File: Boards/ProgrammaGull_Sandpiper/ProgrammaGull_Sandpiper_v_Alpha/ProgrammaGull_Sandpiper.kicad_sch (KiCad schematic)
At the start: 190 parts, among them J4 Conn_01x22_Socket, P1 USB_C_Plug_USB2.0, Q1 MMBT2907, Q2 MMBT2907, Q3 MMBT2907, Q4 MMBT2907, Q5 MMBT2907, Q6 MMBT2907, Q7 MMBT2907, Q8 MMBT2907, SW10 SW_Push, SW11 SW_Push, SW12 SW_Push, SW14 SW_Push, SW9 SW_Push, U1 ICE40UP5K-SG48ITR, U11 ADC084S051CIMM/NOPB, U12 74HC596, U13 74AHC595, U14 W25Q32JVSS, U15 AMS1117-3.3, U2 SN74LVC1G126DCKR, U3 74HC596, U4 MIC5504-1.2YM5, U5 MIC5504-2.5YM5, U6 93LCxxAxxOT, U7 FT2232HQ, X1 SG-210STF

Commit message: Final Alpha Version
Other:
- note added: "Digikey/Mouser: CLMVC-FKA-CLBDGL7LBB79353 JLC/LCSC Option: NH-Z1921RGBA-SF"
- note added: "JLC/LCSC Alternate: YM4012M00033T8188099"
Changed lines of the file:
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@@
+    (effects (font (size 1.27 1.27)) (justify left bottom))
+  )
+  (text "Digikey/Mouser: CLMVC-FKA-CLBDGL7LBB79353\nJLC/LCSC Option: NH-Z1921RGBA-SF"
+    (at 17.78 332.74 0)
     (effects (font (size 1.27 1.27)) (justify left bottom))
   )
@@
     (effects (font (size 3 3)) (justify left bottom))
   )
+  (text "JLC/LCSC Alternate: YM4012M00033T8188099" (at 575.31 99.06 0)
+    (effects (font (size 1.27 1.27)) (justify left bottom))
+  )
   (text "D Pad" (at 405.13 266.065 0)

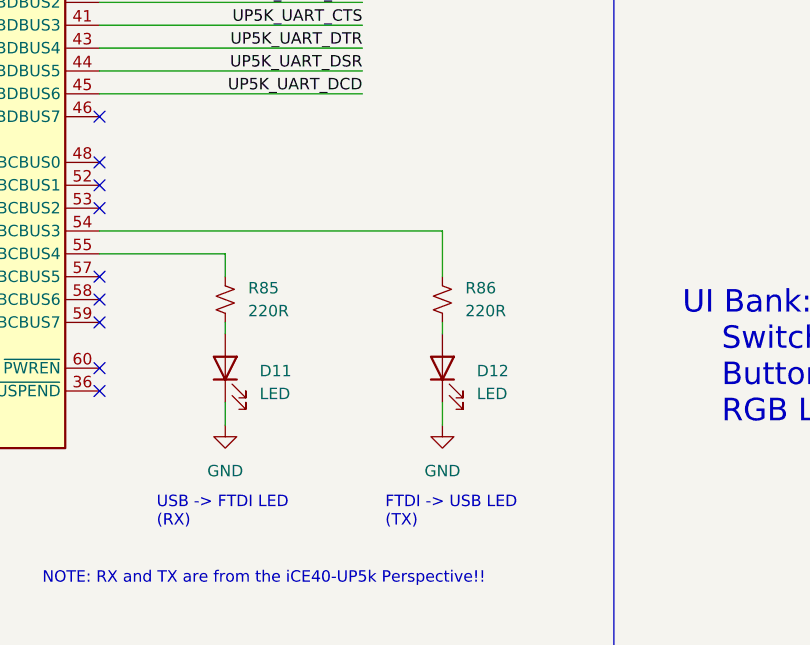
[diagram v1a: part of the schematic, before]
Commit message: Errata: Fixed reversed LEDs on FTDI.... oops :)
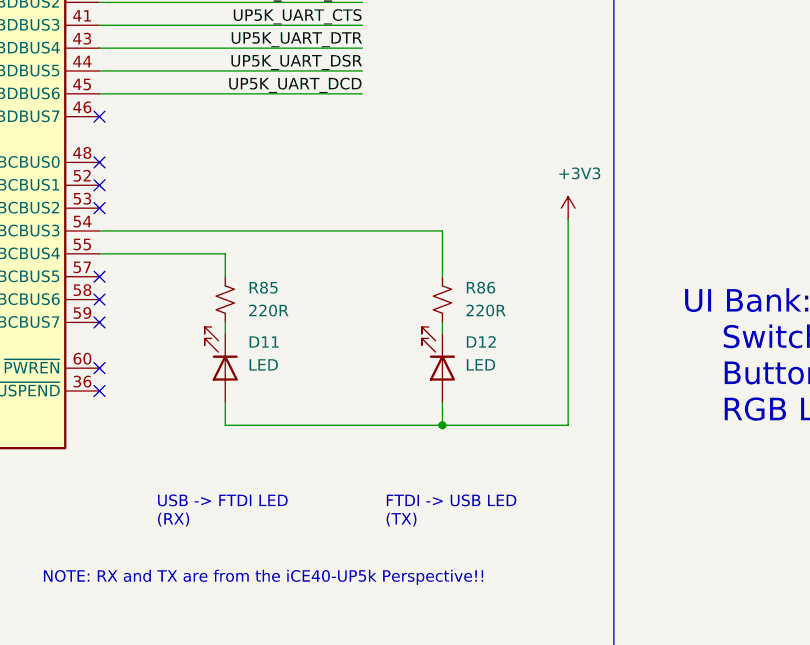
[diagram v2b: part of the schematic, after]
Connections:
- net +3V3: now also D11.2 (A), D12.2 (A)
- net GND: no longer D11.1 (K), D12.1 (K)
- net at R86.1: now also D12.1 (K); no longer D12.2 (A)
- net at R85.1: now also D11.1 (K); no longer D11.2 (A)
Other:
- moved on the sheet: D11, D12
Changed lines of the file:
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@@
   (junction (at 179.07 125.73) (diameter 0) (color 0 0 0 0)
   )
+  (junction (at 234.95 254) (diameter 0) (color 0 0 0 0)
+  )
   (junction (at 351.79 365.76) (diameter 0) (color 0 0 0 0)
   )
@@
     (stroke (width 0) (type default))
   )
+  (wire (pts (xy 248.92 254) (xy 234.95 254))
+    (stroke (width 0) (type default))
+  )
   (polyline (pts (xy 575.31 393.7) (xy 685.8 393.7))
     (stroke (width 0) (type default))
@@
     (stroke (width 0) (type default))
   )
+  (wire (pts (xy 234.95 254) (xy 210.82 254))
+    (stroke (width 0) (type default))
+  )
   (wire (pts (xy 631.19 373.38) (xy 631.19 368.3))
     (stroke (width 0) (type default))
@@
     (stroke (width 0) (type default))
   )
+  (wire (pts (xy 248.92 231.14) (xy 248.92 254))
+    (stroke (width 0) (type default))
+  )
   (wire (pts (xy 407.67 72.39) (xy 407.67 69.85))
     (stroke (width 0) (type default))
@@
     )
   )
-  (symbol (lib_id "power:GND") (at 210.82 254 0) (unit 1)
-    (in_bom yes) (on_board yes) (dnp no) (fields_autoplaced)
-    (property "Reference" "#PWR0160" (at 210.82 260.35 0)
-      (effects (font (size 1.27 1.27)) hide)
-    )
-    (property "Value" "GND" (at 210.82 259.08 0)
-      (effects (font (size 1.27 1.27)))
-    )
-    (property "Footprint" "" (at 210.82 254 0)
-      (effects (font (size 1.27 1.27)) hide)
-    )
-    (property "Datasheet" "" (at 210.82 254 0)
-      (effects (font (size 1.27 1.27)) hide)
-    )
-    (pin "1")
-    (instances
-      (project "ProgrammaGull_Sandpiper"
-        (path "/f134a88c-f9b0-4cfc-ac14-255bf2820348"
-          (reference "#PWR0160") (unit 1)
-        )
-      )
-    )
-  )
   (symbol (lib_id "Device:R_Small_US") (at 478.79 186.69 270) (mirror x) (unit 1)
     (in_bom yes) (on_board yes) (dnp no) (fields_autoplaced)
@@
     )
   )
-  (symbol (lib_id "Device:LED") (at 234.95 247.65 90) (unit 1)
+  (symbol (lib_id "Device:LED") (at 234.95 247.65 270) (unit 1)
     (in_bom yes) (on_board yes) (dnp no) (fields_autoplaced)
-    (property "Reference" "D12" (at 238.76 247.9675 90)
-      (effects (font (size 1.27 1.27)) (justify right))
+    (property "Reference" "D12" (at 237.49 244.7925 90)
+      (effects (font (size 1.27 1.27)) (justify left))
     )
-    (property "Value" "LED" (at 238.76 250.5075 90)
-      (effects (font (size 1.27 1.27)) (justify right))
+    (property "Value" "LED" (at 237.49 247.3325 90)
+      (effects (font (size 1.27 1.27)) (justify left))
     )
     (property "Footprint" "LED_SMD:LED_0805_2012Metric" (at 234.95 247.65 0)
@@
     )
   )
-  (symbol (lib_id "power:GND") (at 234.95 254 0) (unit 1)
-    (in_bom yes) (on_board yes) (dnp no) (fields_autoplaced)
-    (property "Reference" "#PWR0162" (at 234.95 260.35 0)
-      (effects (font (size 1.27 1.27)) hide)
-    )
-    (property "Value" "GND" (at 234.95 259.08 0)
-      (effects (font (size 1.27 1.27)))
-    )
-    (property "Footprint" "" (at 234.95 254 0)
-      (effects (font (size 1.27 1.27)) hide)
-    )
-    (property "Datasheet" "" (at 234.95 254 0)
-      (effects (font (size 1.27 1.27)) hide)
-    )
-    (pin "1")
-    (instances
-      (project "ProgrammaGull_Sandpiper"
-        (path "/f134a88c-f9b0-4cfc-ac14-255bf2820348"
-          (reference "#PWR0162") (unit 1)
-        )
-      )
-    )
-  )
   (symbol (lib_id "Device:R_Small_US") (at 322.58 302.26 180) (unit 1)
     (in_bom yes) (on_board yes) (dnp no) (fields_autoplaced)
@@
     )
   )
-  (symbol (lib_id "Device:LED") (at 210.82 247.65 90) (unit 1)
+  (symbol (lib_id "Device:LED") (at 210.82 247.65 270) (unit 1)
     (in_bom yes) (on_board yes) (dnp no) (fields_autoplaced)
-    (property "Reference" "D11" (at 214.63 247.9675 90)
-      (effects (font (size 1.27 1.27)) (justify right))
+    (property "Reference" "D11" (at 213.36 244.7925 90)
+      (effects (font (size 1.27 1.27)) (justify left))
     )
-    (property "Value" "LED" (at 214.63 250.5075 90)
-      (effects (font (size 1.27 1.27)) (justify right))
+    (property "Value" "LED" (at 213.36 247.3325 90)
+      (effects (font (size 1.27 1.27)) (justify left))
     )
     (property "Footprint" "LED_SMD:LED_0805_2012Metric" (at 210.82 247.65 0)
@@
         )
       )
+    )
+  )
+  (symbol (lib_id "power:+3V3") (at 248.92 231.14 0) (unit 1)
+    (in_bom yes) (on_board yes) (dnp no)
+    (property "Reference" "#PWR018" (at 248.92 234.95 0)
+      (effects (font (size 1.27 1.27)) hide)
+    )
+    (property "Value" "+3V3" (at 250.19 226.06 0)
+      (effects (font (size 1.27 1.27)))
+    )
+    (property "Footprint" "" (at 248.92 231.14 0)
+      (effects (font (size 1.27 1.27)) hide)
+    )
+    (property "Datasheet" "" (at 248.92 231.14 0)
+      (effects (font (size 1.27 1.27)) hide)
+    )
+    (pin "1")
+    (instances
+      (project "ProgrammaGull_Sandpiper"
+        (path "/f134a88c-f9b0-4cfc-ac14-255bf2820348"
+          (reference "#PWR018") (unit 1)
+        )
+      )

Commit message: Converted to 3v3 7 segment drive voltage
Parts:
- R2, R35, R54, R87, R88, R89, R90, R91: value 680R -> 2k2
- R43, R44, R45, R46, R47, R48, R49, R50: value 383R -> 150R
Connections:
- net +3V3: now also Q1.2 (E), Q2.2 (E), Q3.2 (E), Q4.2 (E), Q5.2 (E), Q6.2 (E), Q7.2 (E), Q8.2 (E), R67.2, R68.2, R69.2, R70.2, R71.2, R72.2, R73.2, R74.2
- net +5V: no longer Q1.2 (E), Q2.2 (E), Q3.2 (E), Q4.2 (E), Q5.2 (E), Q6.2 (E), Q7.2 (E), Q8.2 (E), R67.2, R68.2, R69.2, R70.2, R71.2, R72.2, R73.2, R74.2
